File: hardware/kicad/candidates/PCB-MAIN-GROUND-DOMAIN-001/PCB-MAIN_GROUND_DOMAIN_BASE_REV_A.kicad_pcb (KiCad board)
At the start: 6 copper layers, 110 x 75 mm, 251 parts, among them J10 U.FL-R-SMT-1(60), J11 USB4105-GF-A-120, J12 MEM2052-00-195-00-A, J13 504050-0291, J6 2336582-1, J7 2336582-1, J8 U.FL-R-SMT-1(60), J9 U.FL-R-SMT-1(60), Q1 MMBT3904,215, Q2 MMBT3904,215, Q3 MMBT3904,215, Q4 Si1016X-T1-GE3, U1 STM32U585VIT6Q, U10 E22-900M22S, U11 MDBT50Q-P1MV2, U13 TS3A27518EPWR, U14 ESDALC6V1-5P6, U15 ESDALC6V1-5P6, U16 SN74AXC8T245PWR, U17 SN74LVC32APWR, U18 SN74AXC1T45DRLR, U19 TPD4E05U06DQAR, U2 W25Q512JVFIQ, U20 TPD4E05U06DQAR, U21 TPD4E05U06DQAR, U22 TPD4E05U06DQAR, U23 TPD4E05U06DQAR, U24 TPD4E05U06DQAR, U25 TPD2EUSB30DRTR, U26 TPD2EUSB30DRTR, U27 TPD4E05U06DQAR, U3 LIS2DW12TR, U4 STTS22HTR, U5 LT6000IDCB#TRMPBF, U6 SN74LVC1G07DBVR, U7 SN74AXC8T245PWR, U8 BG95-M3, U9 MAX-M10S-00B, X1 SiT1552AI-JE-DCC-32.768D

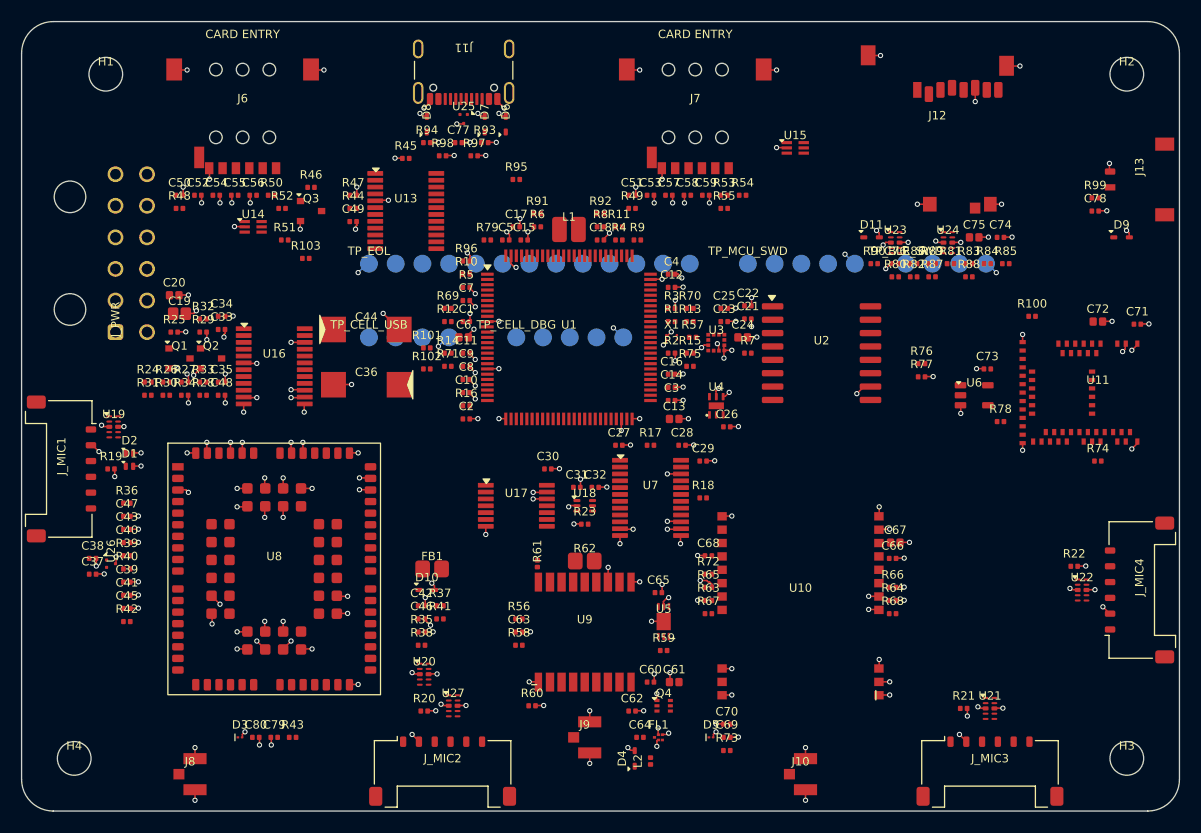
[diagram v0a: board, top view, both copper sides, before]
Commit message: hardware: apply PCB-MAIN ground-domain routing subgate
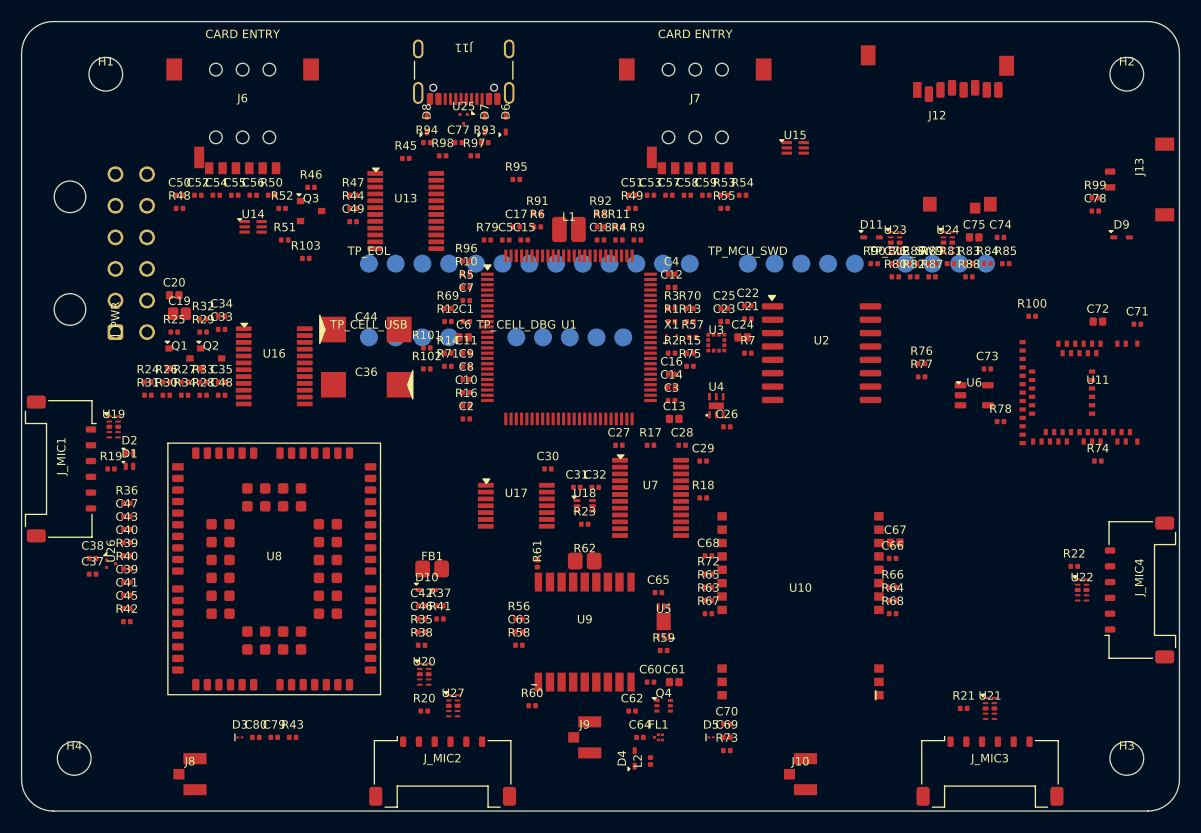
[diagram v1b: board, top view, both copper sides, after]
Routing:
- net GND_DIGITAL: track 120.4 -> 0.00 mm, vias 138 -> 0
- net GND_MODEM: track 88.6 -> 0.00 mm, vias 95 -> 0
- net GND_MIC: track 17.5 -> 0.00 mm, vias 21 -> 0
- removed copper zone on In1.Cu, net GND_DIGITAL
- removed copper zone on In2.Cu, net GND_MIC
- removed copper zone on In4.Cu, net GND_MODEM
